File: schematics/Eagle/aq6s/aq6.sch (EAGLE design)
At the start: 5 parts

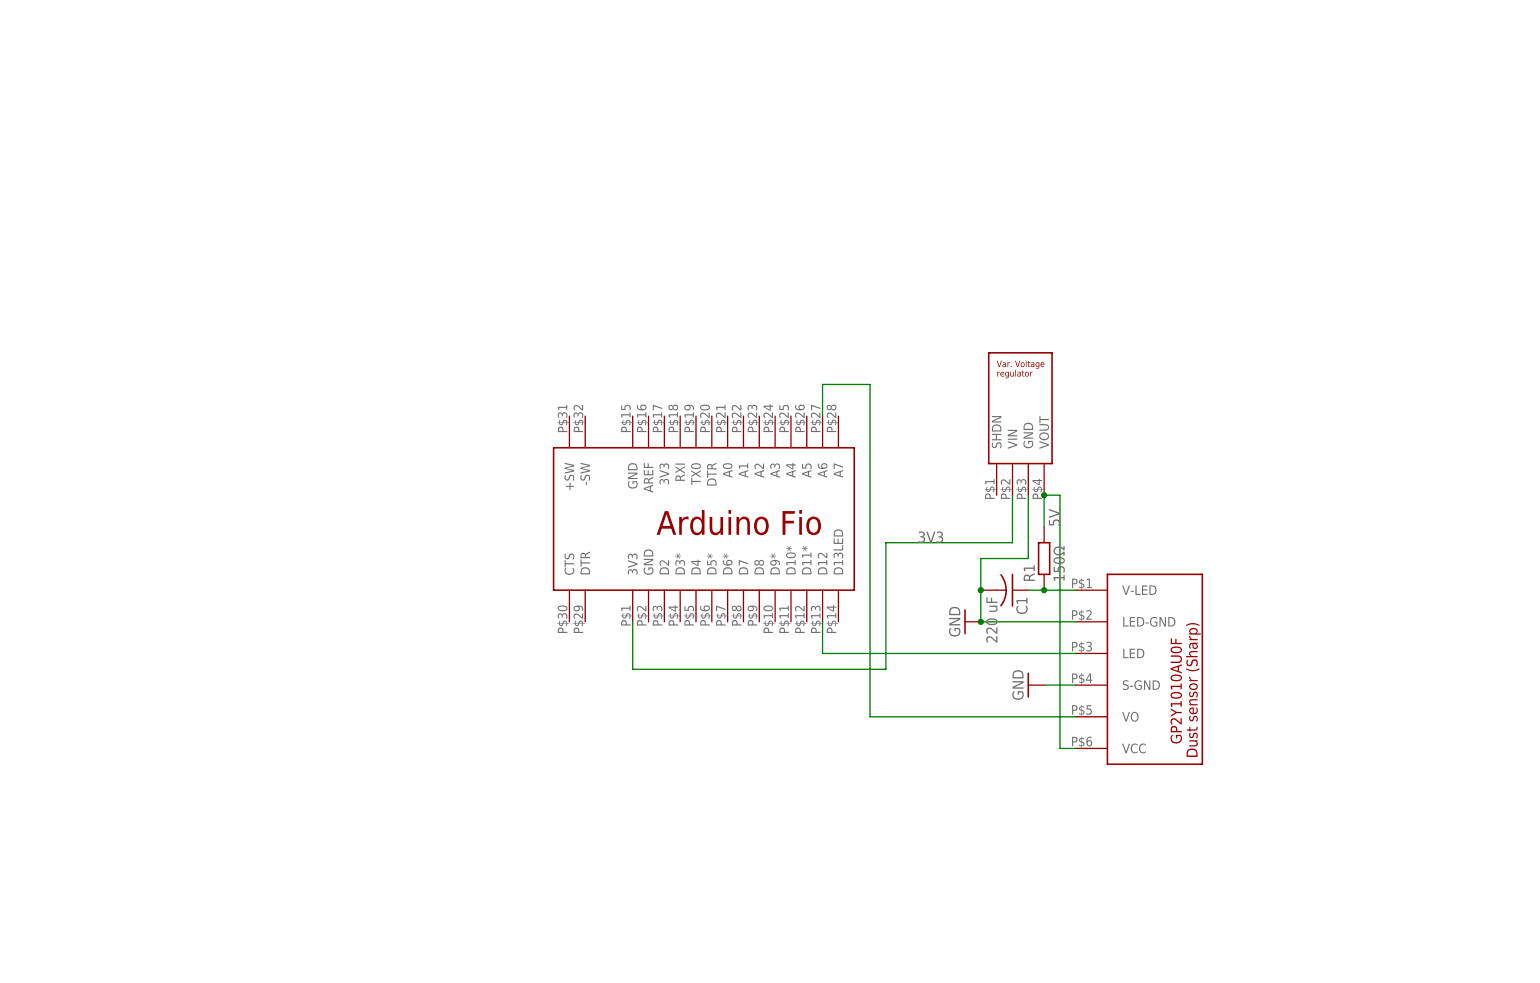
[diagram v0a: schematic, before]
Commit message: Added more components to Eagle schematic, library
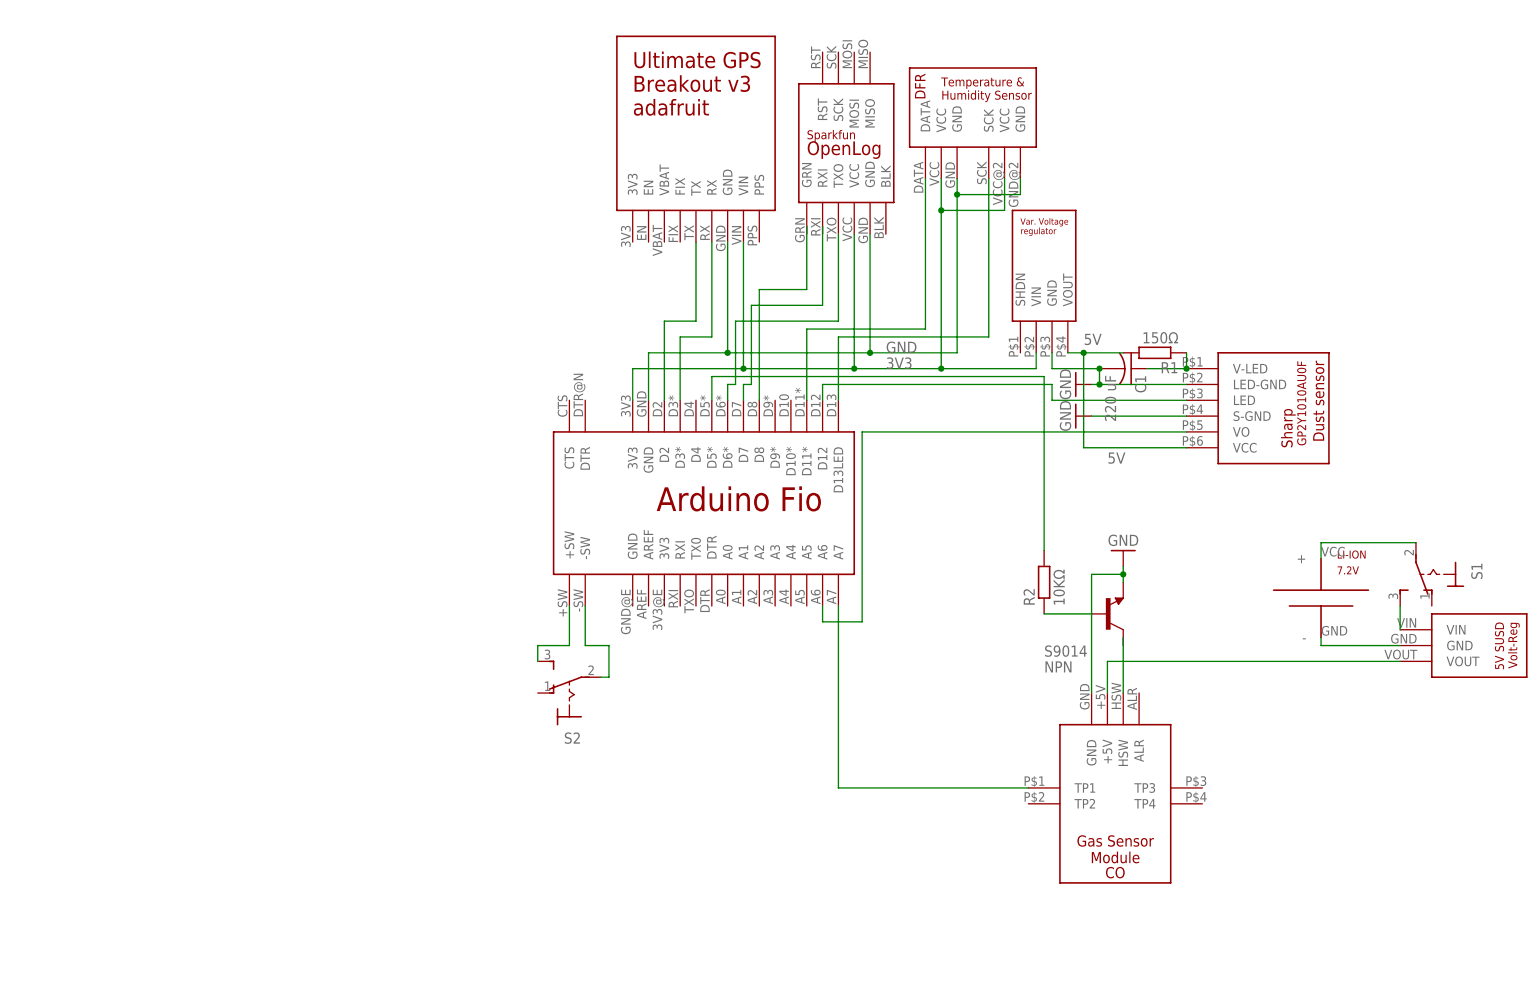
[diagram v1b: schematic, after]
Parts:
- added CO: CO, air_quality_parts:CO
- added LI-ION: 7.2V, air_quality_parts:BATTERY_WITH_PCB_HOLES
- added NPN: S9014, transistor:-NPN-TO92-E1
- added R2: 10KΩ, resistor:R-EU_0204/7
- added S1, S2: (no value), switch:M9040P
- added U$4: ADAFRUIT_GPS_V3, air_quality_parts:ADAFRUIT_GPS_V3
- added U$5: SPARKFUN_OPENLOG, air_quality_parts:SPARKFUN_OPENLOG
- added U$6: DFR_TEMP_HUMIDITY, air_quality_parts:DFR_TEMP_HUMIDITY
- added U$7: 5V_SUSD_VOLT_REG, air_quality_parts:5V_SUSD_VOLT_REG
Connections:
- new net N$10: S2.P, U$2.-SW
- new net N$11: LI-ION.+, S1.P
- new net N$12: U$2.D13LED, U$6.SCK
- new net N$13: U$2.D11*, U$6.DATA
- new net N$14: S1.S, U$7.VIN
- new net N$15: LI-ION.-, U$7.GND
- new net N$16: NPN.B, R2.1
- new net N$17: R2.2, U$2.D5*
- new net N$18: CO.+5V, U$7.VOUT
- new net N$19: CO.HSW
- new net N$20: CO.TP1, U$2.A7
- new net N$4: U$2.D3*, U$4.RX
- new net N$5: U$2.D2, U$4.TX
- new net N$6: S2.S, U$2.+SW
- new net N$7: U$2.D8
- new net N$8: U$2.D7
- new net N$9: U$2.D6*, U$5.TXO
- net 3V3: now also U$4.VIN, U$5.VCC, U$6.VCC, U$6.VCC@2
- net GND: now also CO.GND, NPN.E, U$2.GND, U$4.GND, U$5.GND, U$6.GND, U$6.GND@2
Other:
- moved on the sheet: C1, R1

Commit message: Finished circuit diagram, needs checking
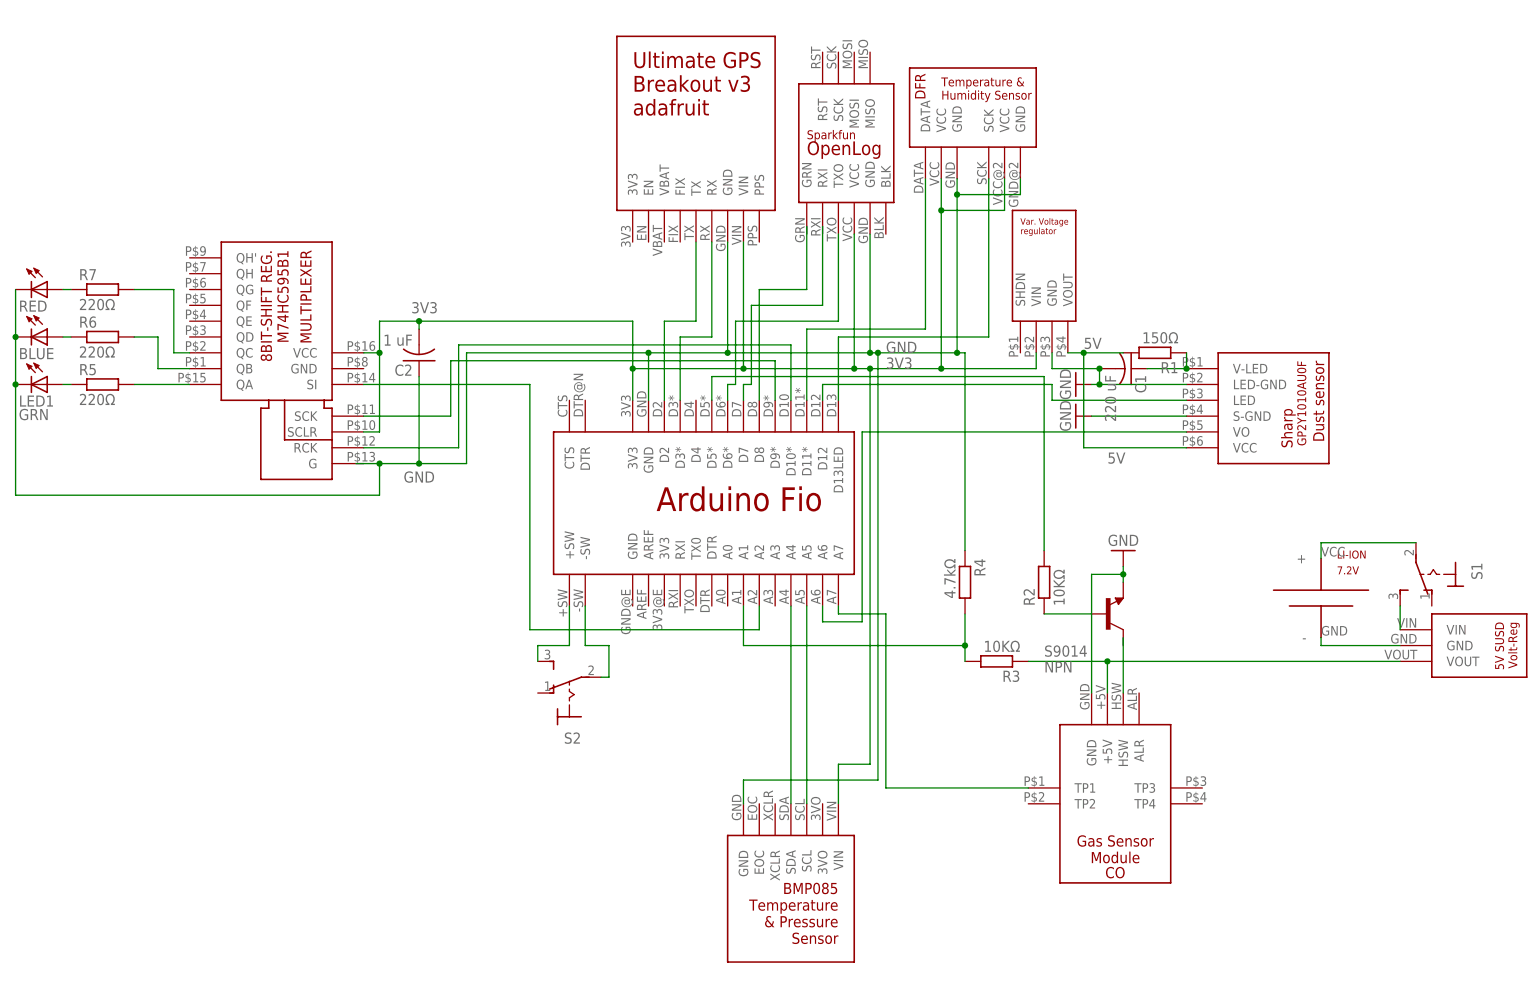
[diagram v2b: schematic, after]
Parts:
- added BLUE, RED: (no value), adafruit:LED5MM
- added C2: 1 uF, resistor:C-US050-025X075
- added LED1: GRN, adafruit:LED5MM
- added R3: 10KΩ, resistor:R-EU_0204/7
- added R4: 4.7kΩ, resistor:R-EU_0204/7
- added R5, R6, R7: 220Ω, resistor:R-EU_0204/7
- added U$8: BMP085, air_quality_parts:BMP085
- added U$9: M74HC595B1, air_quality_parts:M74HC595B1
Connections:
- new net N$21: R3.2, R4.2, U$2.A1
- new net N$22: U$2.A2, U$9.SI
- new net N$23: U$2.A5, U$8.SCL
- new net N$24: U$2.A4, U$8.SDA
- new net N$25: R5.2, U$9.QA
- new net N$26: U$2.D9*, U$9.SCK
- new net N$27: U$2.D10*, U$9.RCK
- new net N$28: R7.2, U$9.QC
- new net N$29: R6.2, U$9.QB
- new net N$30: R7.1, RED.A
- new net N$31: BLUE.A, R6.1
- new net N$32: LED1.A, R5.1
- net 3V3: now also C2.2, U$8.VIN, U$9.SCLR, U$9.VCC
- net GND: now also BLUE.C, C2.1, LED1.C, R4.1, RED.C, U$8.GND
- net N$18: now also R3.1

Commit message: PCB layout tentatively ok, routing next
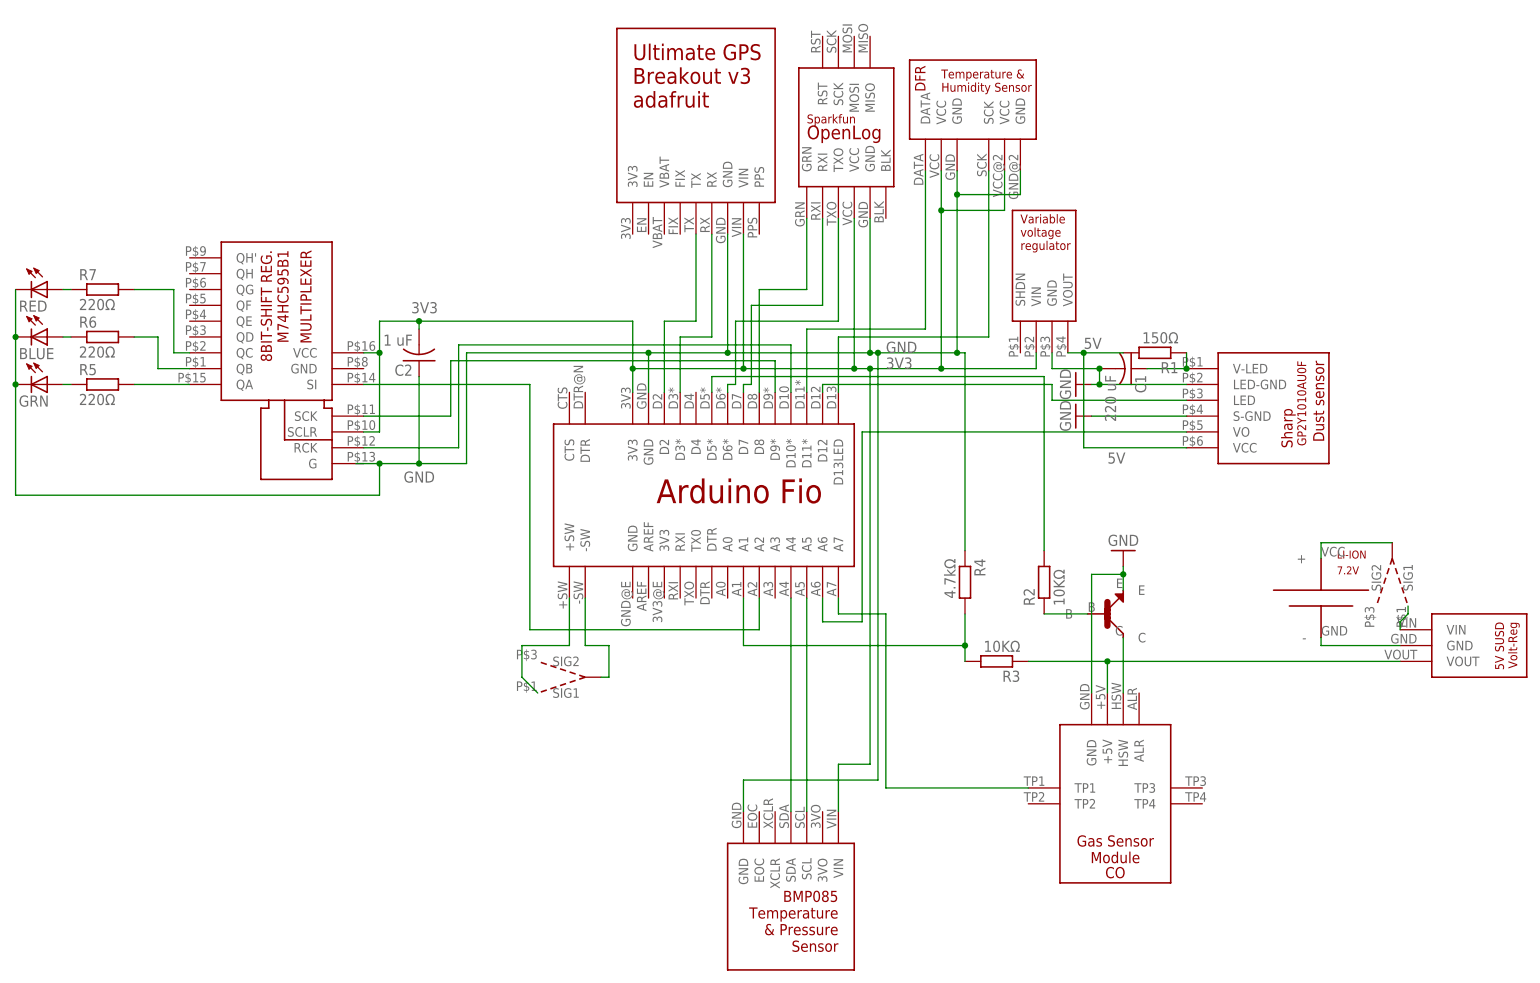
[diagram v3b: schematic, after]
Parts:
- removed NPN: S9014, transistor:-NPN-TO92-E1
- removed S1, S2: (no value), switch:M9040P
- added U$10, U$11: SWITCH, air_quality_parts:SWITCH
- added U$12: NPN, air_quality_parts:NPN
- GRN: value GRN -> (none)
- renumbered LED1 to GRN
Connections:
- net GND: now also U$12.E; no longer NPN.E
- net N$10: now also U$10.SIG_OUT; no longer S2.P
- net N$11: now also U$11.SIG_OUT; no longer S1.P
- net N$14: now also U$11.SIG1; no longer S1.S
- net N$16: now also U$12.B; no longer NPN.B
- net N$19: now also U$12.C
- net N$6: now also U$10.SIG1; no longer S2.S
- net N$7: now also U$5.GRN
- net N$8: now also U$5.RXI

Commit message: PCB first draft, needs checking and adjustment
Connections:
- net GND: now also U$9.G
- net N$12: now also U$2.D4; no longer U$2.D13LED
- net N$13: now also U$2.D5*; no longer U$2.D11*
- net N$17: now also U$2.D11*; no longer U$2.D5*
- net N$21: now also U$2.A3; no longer U$2.A1
- net N$22: now also U$2.A1; no longer U$2.A2
- net N$23: now also U$2.A4; no longer U$2.A5
- net N$24: now also U$2.A5; no longer U$2.A4
- net N$25: now also U$9.QB; no longer U$9.QA
- net N$26: now also U$2.D10*; no longer U$2.D9*
- net N$27: now also U$2.D9*; no longer U$2.D10*
- net N$28: now also U$9.QD; no longer U$9.QC
- net N$29: now also U$9.QC; no longer U$9.QB
- net N$7: now also U$2.D6*; no longer U$2.D8
- net N$9: now also U$2.D8; no longer U$2.D6*
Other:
- moved on the sheet: C2
